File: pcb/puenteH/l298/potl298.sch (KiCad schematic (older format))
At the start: 19 parts, among them K1 CONN_3, K2 CONN_3, P1 CONN_2X2, P2 v10, P3 CONN_2, P4 CONN_2, U1 L298

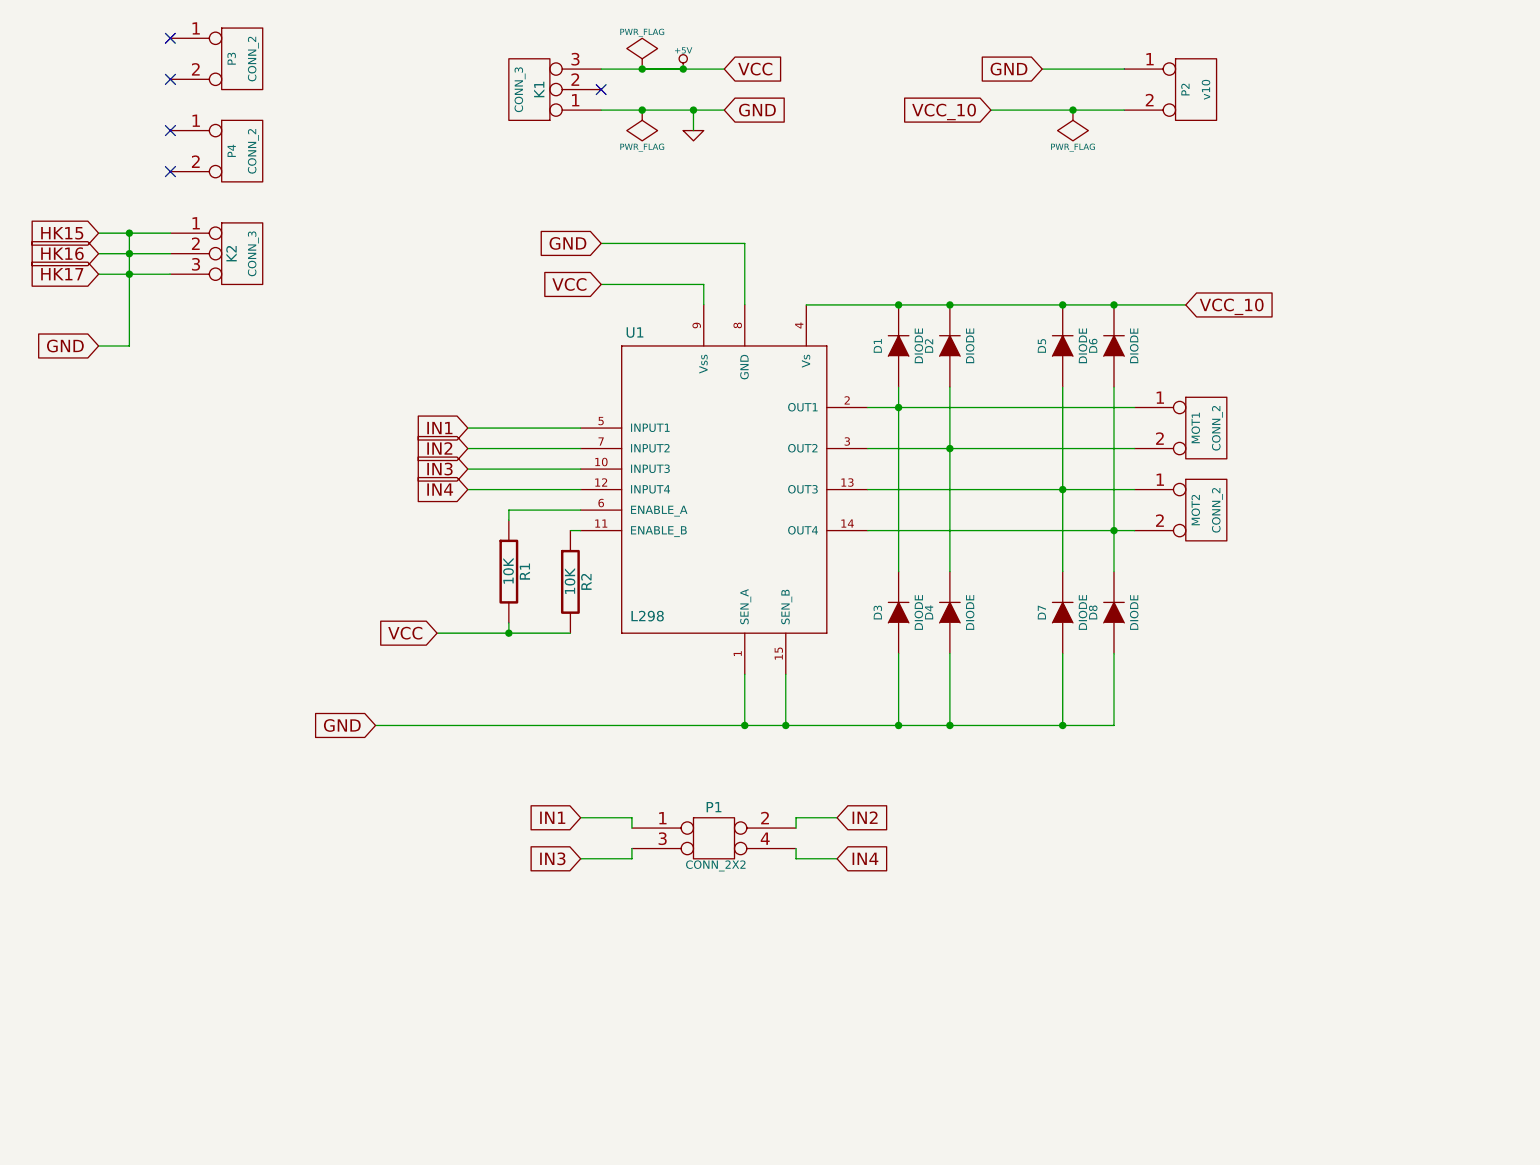
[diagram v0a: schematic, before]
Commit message: H bridge L298 completed for connect to usb4butia (version 1.8.9 and futures)
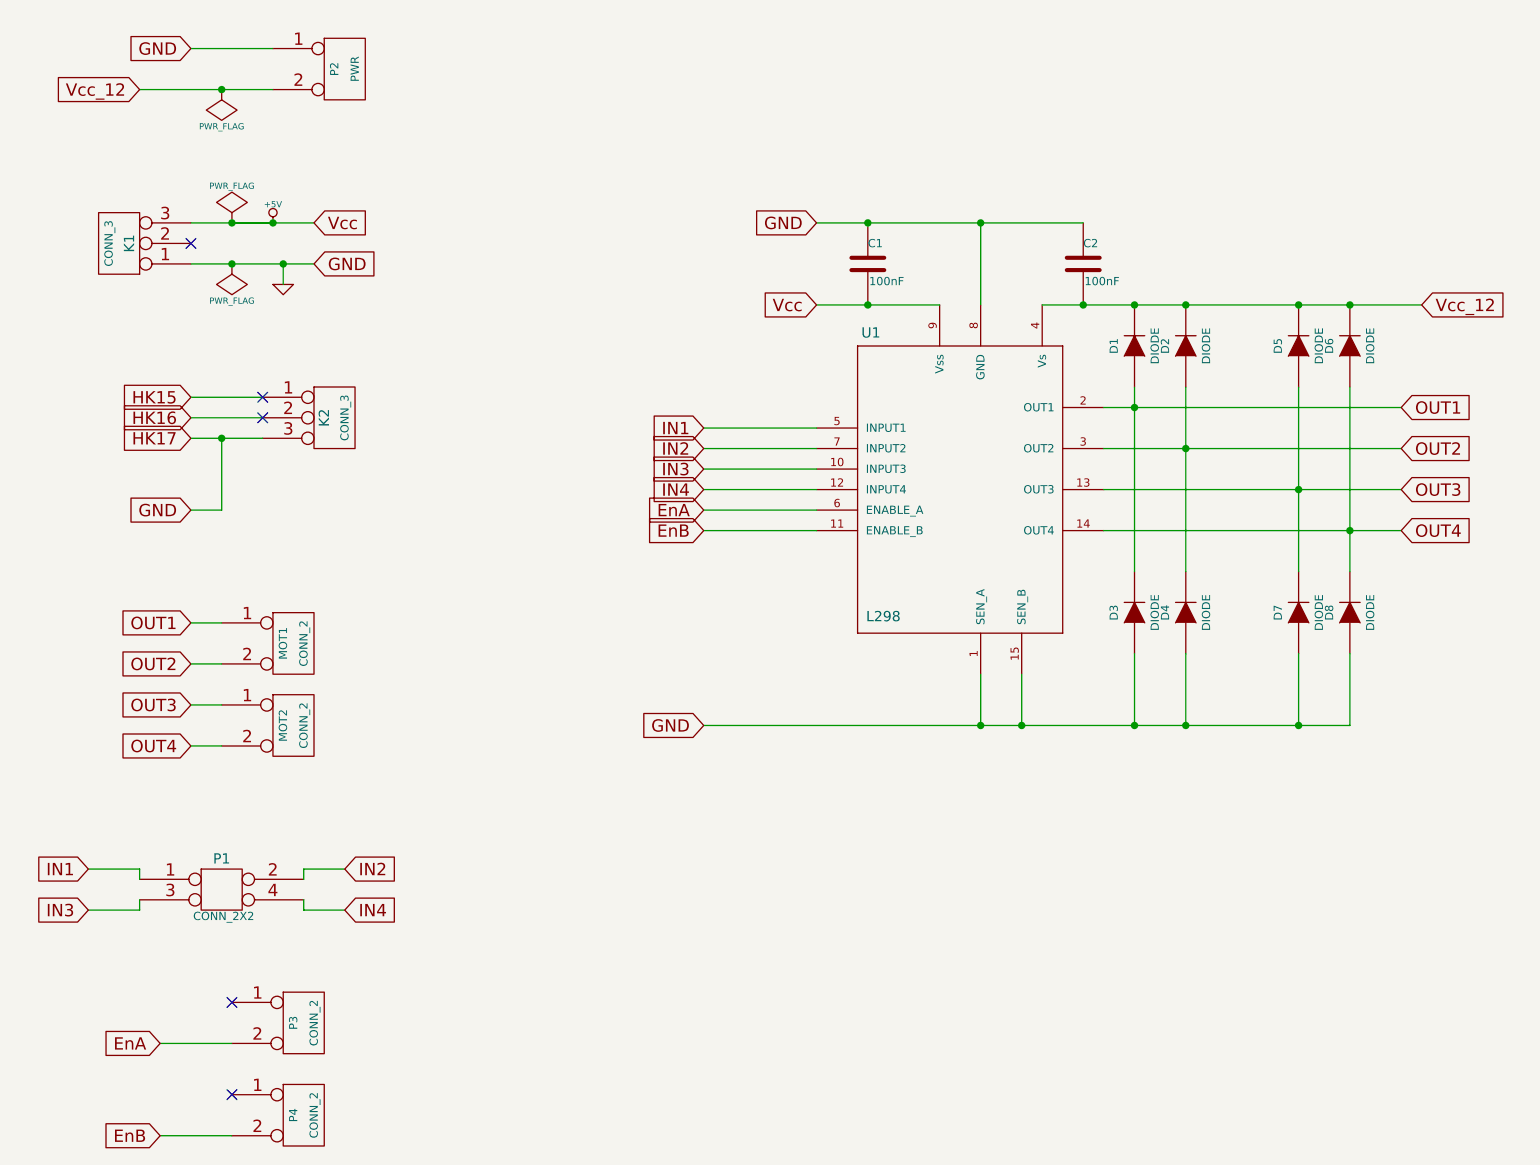
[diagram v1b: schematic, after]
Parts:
- removed R1, R2: 10K, symbol R
- added C1, C2: 100nF, ~, symbol C
- P2: value v10 -> PWR
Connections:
- net +5V: now also C1.2
- net GND: now also C1.1, C2.1; no longer K2.1 (P1), K2.2 (PM)
- net OUT1: now reaches D1.1 (A), D3.2 (K), MOT1.1 (P1), U1.2 (OUT1)
- net OUT2: now reaches D2.1 (A), D4.2 (K), MOT1.2 (PM), U1.3 (OUT2)
- net OUT3: now reaches D5.1 (A), D7.2 (K), MOT2.1 (P1), U1.13 (OUT3)
- net OUT4: now reaches D6.1 (A), D8.2 (K), MOT2.2 (PM), U1.14 (OUT4)
- net EnA: now reaches U1.6 (ENABLE_A)
- net EnA: now also P3.2 (PM)
- net EnB: now reaches U1.11 (ENABLE_B)
- net EnB: now also P4.2 (PM)
- net VCC_10 renamed Vcc_12
- net Vcc_12: now also C2.2
- new net HK15: K2.1 (P1)
- new net HK16: K2.2 (PM)
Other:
- moved on the sheet: D1, D2, D3, D4, D5, D6, D7, D8, K1, K2, MOT1, MOT2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
